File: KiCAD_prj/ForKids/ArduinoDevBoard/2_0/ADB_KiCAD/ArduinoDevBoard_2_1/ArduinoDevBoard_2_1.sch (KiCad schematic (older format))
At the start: 45 parts, among them J1 Conn_01x04_Female, J10 Conn_01x04_Female, J11 Conn_01x04_Female, J12 Conn_01x02_Female, J13 Conn_01x15_Female, J14 Conn_01x15_Female, J15 Conn_01x03_Female, J16 Conn_01x02_Female, J17 Conn_01x02_Female, J18 Conn_01x02_Female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

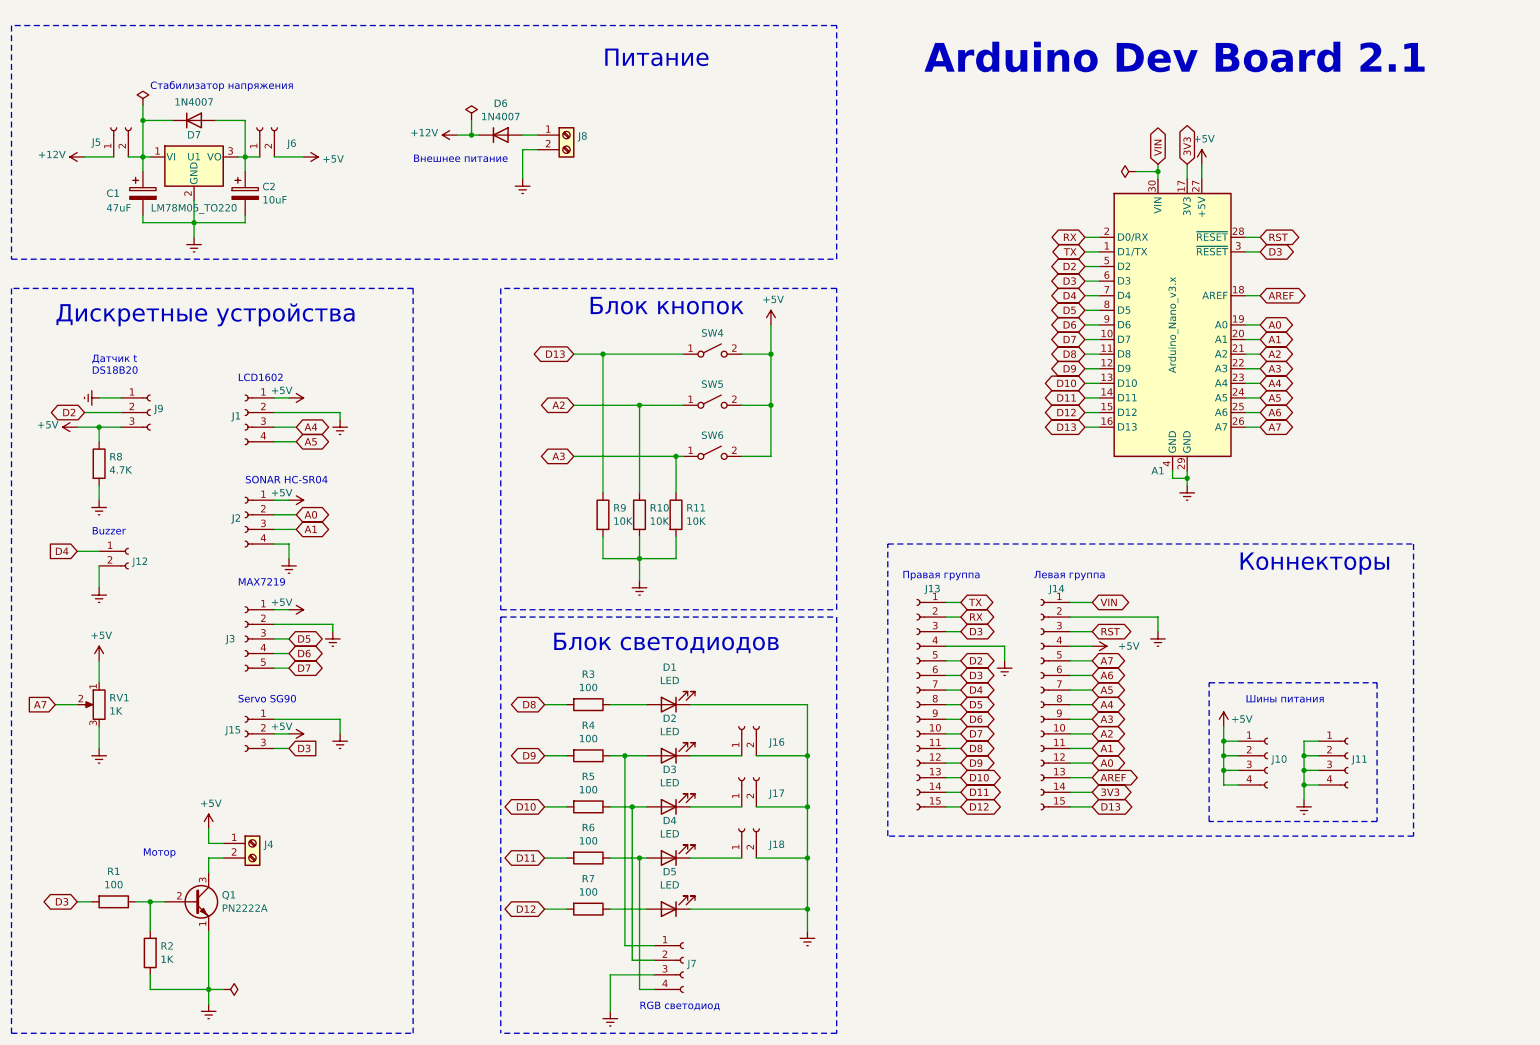
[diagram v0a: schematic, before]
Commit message: Update Arduino Dev Board 2.1
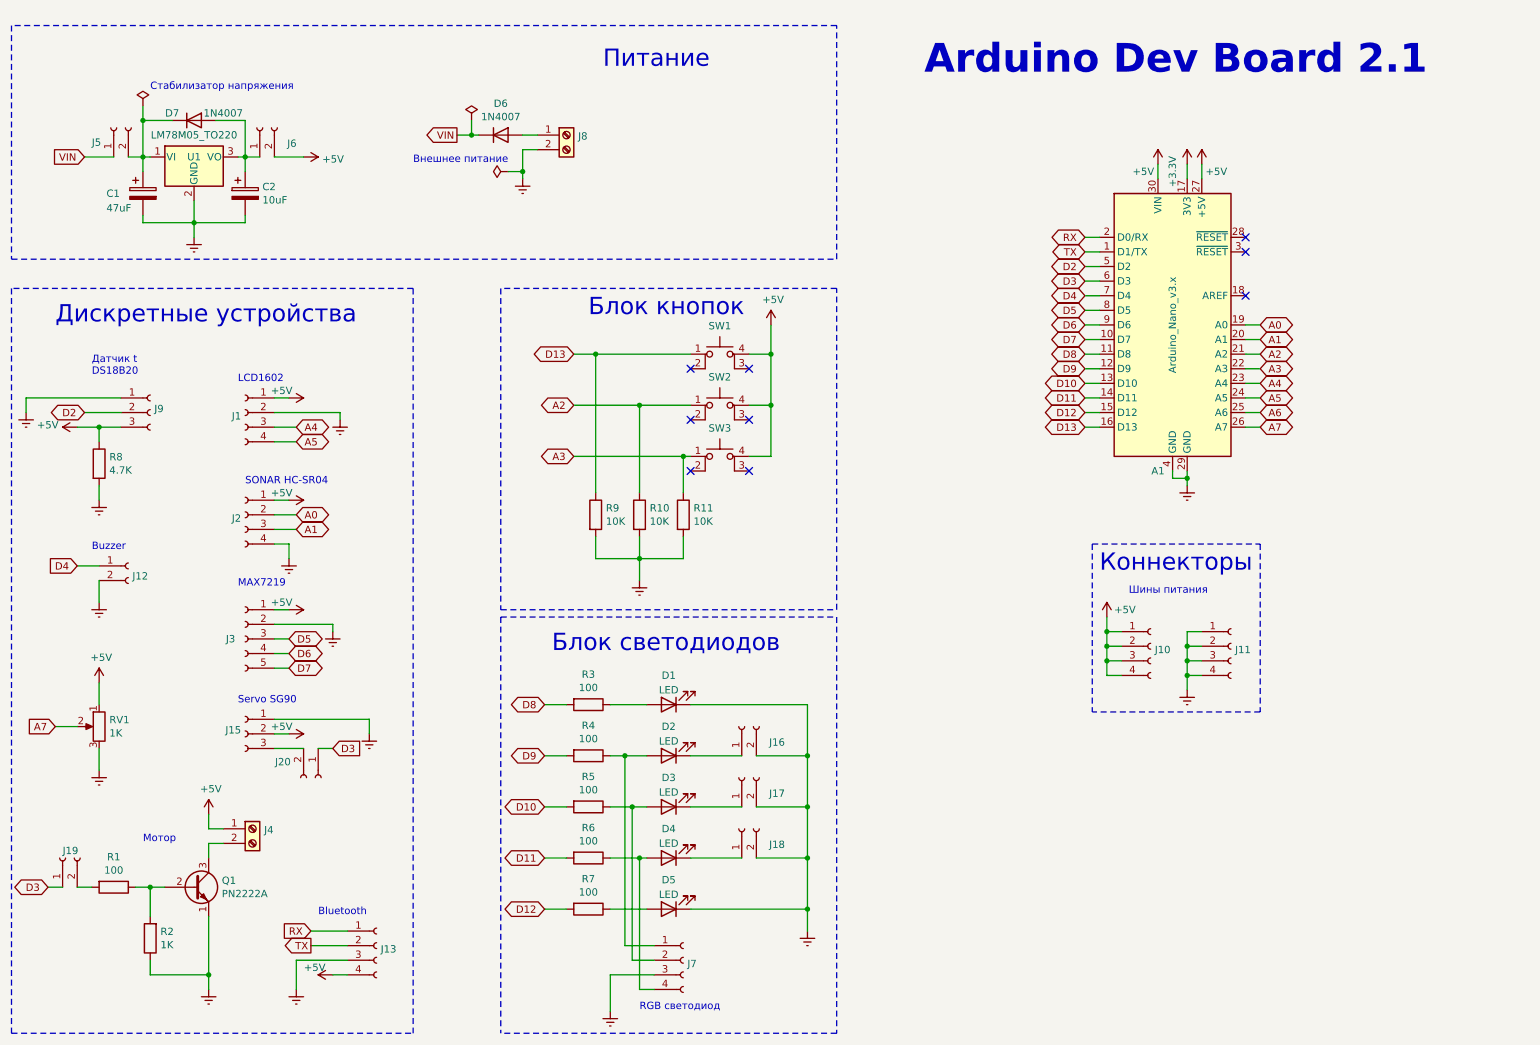
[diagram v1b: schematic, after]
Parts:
- removed J13, J14: Conn_01x15_Female, Connector_PinSocket_2.54mm:PinSocket_1x15_P2.54mm_Vertical, symbol Connector:Conn_01x15_Female
- removed SW4, SW5, SW6: SW_SPST, Button_Switch_THT:SW_PUSH_6mm_H5mm, symbol Switch:SW_SPST
- added J13: Conn_01x04_Female, Connector_PinHeader_2.54mm:PinHeader_1x04_P2.54mm_Vertical, symbol Connector:Conn_01x04_Female
- added J19, J20: Conn_01x02_Female, Connector_PinHeader_2.54mm:PinHeader_1x02_P2.54mm_Vertical, symbol Connector:Conn_01x02_Female
- added SW1, SW2, SW3: Button_Switch_THT:SW_PUSH_6mm_H5mm, Button_Switch_THT:SW_PUSH_6mm, symbol Switch:SW_MEC_5E
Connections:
- net +12V is gone; now on net VIN: D6.1 (K), J5.1 (Pin_1)
- net +5V: now also A1.30 (VIN), J13.4 (Pin_4), SW1.4 (A), SW2.4 (A), SW3.4 (A)
- net A2: now also SW2.1
- net A3: now also SW3.1
- net D13: now also SW1.1
- net D3: now also J19.1 (Pin_1), J20.1 (Pin_1); no longer A1.3 (~RESET), J15.3 (Pin_3), R1.2
- net Earth: now also J13.3 (Pin_3)
- net RX: now also J13.1 (Pin_1)
- net TX: now also J13.2 (Pin_2)
- net VIN: no longer A1.30 (VIN)
- net 3V3 renamed +3V3
- net AREF: no longer names the net of A1.18 (AREF)
- net RST: no longer names the net of A1.28 (~RESET)
- new net: J19.2 (Pin_2), R1.2
- new net: J15.3 (Pin_3), J20.2 (Pin_2)
- no-connect marks 0 -> 9
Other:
- note added: "Bluetooth"
- note removed: "Левая группа"
- note removed: "Правая группа"
- moved on the sheet: J10, J11, J12, J4, Q1, R1, R11, R2, R9, RV1

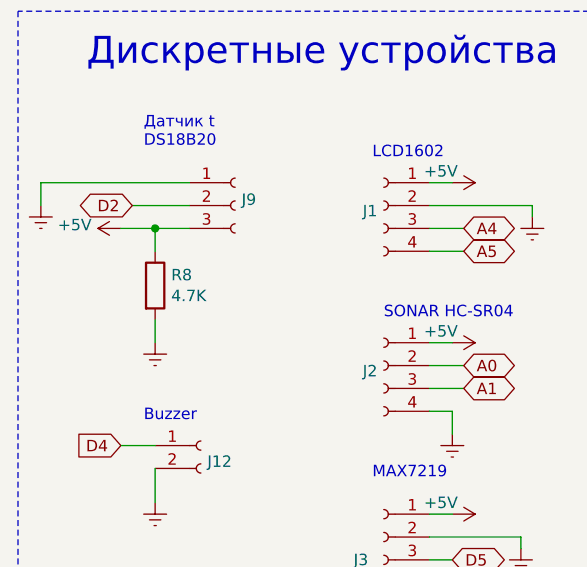
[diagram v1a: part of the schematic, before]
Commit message: Update Arduino Dev Board 2.1 fix resistor 4.7K
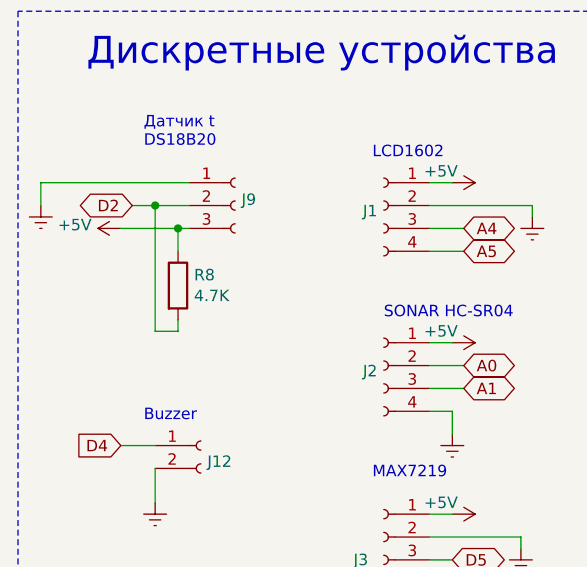
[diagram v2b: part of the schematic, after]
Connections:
- net D2: now also R8.2
- net Earth: no longer R8.2
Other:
- moved on the sheet: R8
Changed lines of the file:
@@
 L Device:R R8
 U 1 1 5DFDE4CA
-P 1600 3700
-F 0 "R8" H 1670 3746 50  0000 L CNN
-F 1 "4.7K" H 1670 3655 50  0000 L CNN
-F 2 "Resistor_THT:R_Axial_DIN0411_L9.9mm_D3.6mm_P12.70mm_Horizontal" V 1530 3700 50  0001 C CNN
-F 3 "~" H 1600 3700 50  0001 C CNN
-	1    1600 3700
-	1    0    0    -1
-$EndComp
-Wire Wire Line
-	1750 3450 1600 3450
-Wire Wire Line
-	1600 3450 1600 3550
+P 1700 3700
+F 0 "R8" H 1770 3746 50  0000 L CNN
+F 1 "4.7K" H 1770 3655 50  0000 L CNN
+F 2 "Resistor_THT:R_Axial_DIN0411_L9.9mm_D3.6mm_P12.70mm_Horizontal" V 1630 3700 50  0001 C CNN
+F 3 "~" H 1700 3700 50  0001 C CNN
+	1    1700 3700
+	1    0    0    -1
+$EndComp
 $Comp
 L power:+5V #PWR019
@@
 	0    -1   -1   0
 $EndComp
-Wire Wire Line
-	1450 3450 1600 3450
-Connection ~ 1600 3450
 Text GLabel 1500 3350 0    50   BiDi ~ 0
 D2
 Wire Wire Line
-	1750 3350 1500 3350
+	1750 3350 1600 3350
 $Comp
 L power:Earth #PWR020
@@
 	9550 2950 9450 2950
 $Comp
-L power:Earth #PWR021
-U 1 1 5E01E177
-P 1600 3950
-F 0 "#PWR021" H 1600 3700 50  0001 C CNN
-F 1 "Earth" H 1600 3800 50  0001 C CNN
-F 2 "" H 1600 3950 50  0001 C CNN
-F 3 "~" H 1600 3950 50  0001 C CNN
-	1    1600 3950
-	1    0    0    -1
-$EndComp
-Wire Wire Line
-	1600 3950 1600 3850
-$Comp
 L Device:LED D1
 U 1 1 5E023966
@@
 	1    0    0    -1
 $EndComp
+Wire Wire Line
+	1450 3450 1700 3450
+Wire Wire Line
+	1700 3550 1700 3450
+Connection ~ 1700 3450
+Wire Wire Line
+	1700 3450 1750 3450
+Wire Wire Line
+	1700 3850 1700 3900
+Wire Wire Line
+	1700 3900 1600 3900
+Wire Wire Line
+	1600 3900 1600 3350
+Connection ~ 1600 3350
+Wire Wire Line
+	1600 3350 1500 3350
 $EndSCHEMATC

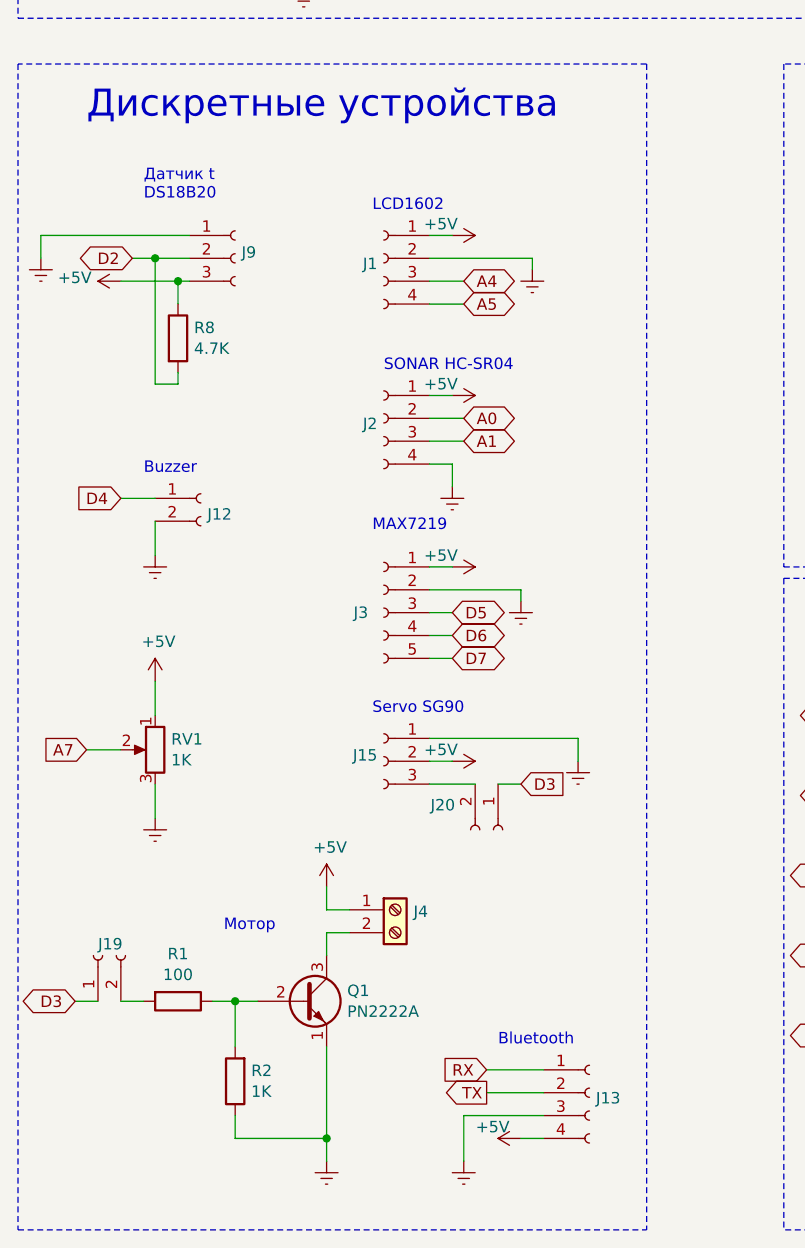
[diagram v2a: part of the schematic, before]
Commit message: Update Arduino Dev Board 2.0 KiCAD project: A6 -> sens t. D2 - free
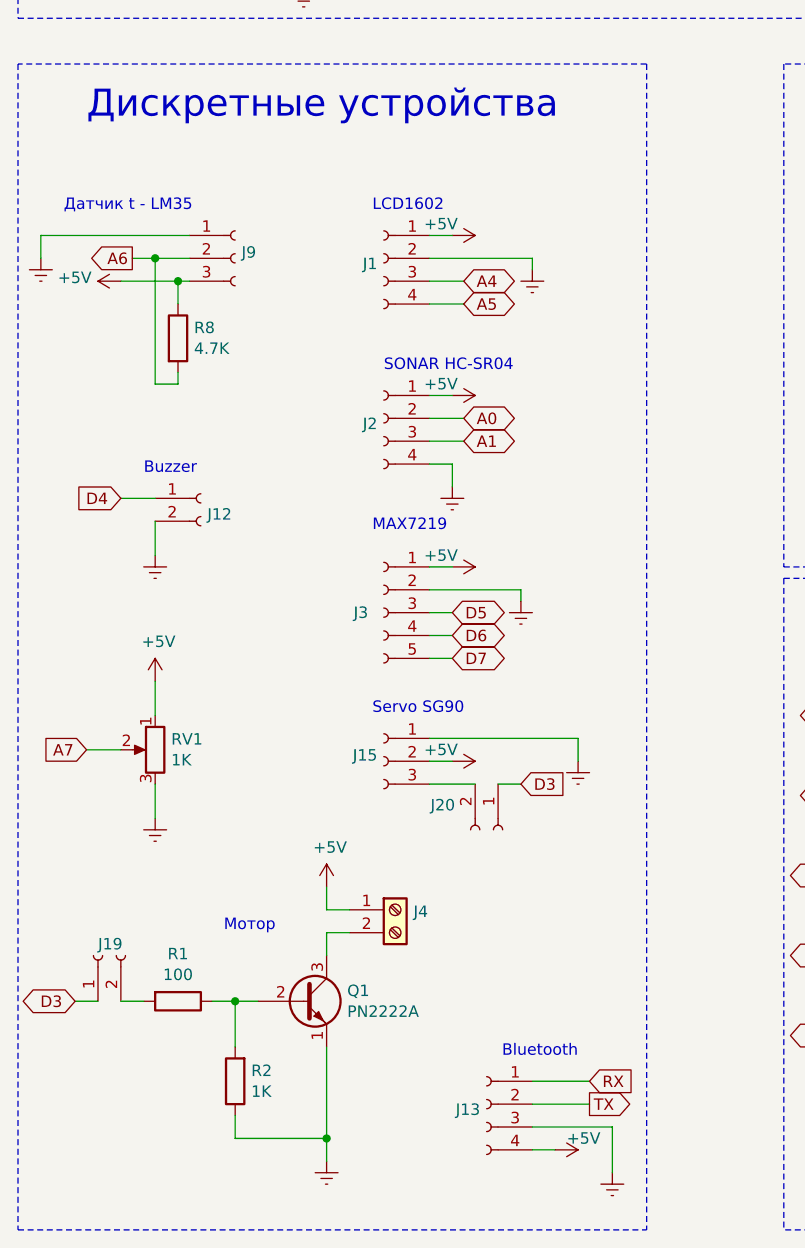
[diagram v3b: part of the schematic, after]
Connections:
- net A6: now also J9.2 (Pin_2), R8.2
- net D2: no longer J9.2 (Pin_2), R8.2
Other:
- note added: "Датчик t - LM35"
- note removed: "Датчик t\nDS18B20"
- moved on the sheet: J13
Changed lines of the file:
@@
 	0    -1   -1   0
 $EndComp
-Text GLabel 1500 3350 0    50   BiDi ~ 0
-D2
 Wire Wire Line
 	1750 3350 1600 3350
@@
 Text Notes 1950 1150 0    50   ~ 0
 Стабилизатор напряжения
-Text Notes 1550 3100 0    50   ~ 0
-Датчик t\nDS18B20
+Text Notes 1200 3150 0    50   ~ 0
+Датчик t - LM35
 $Comp
 L Connector:Screw_Terminal_01x02 J8
@@
 L Connector:Conn_01x04_Female J13
 U 1 1 60046ECC
-P 3500 7000
-F 0 "J13" H 3528 6976 50  0000 L CNN
-F 1 "Conn_01x04_Female" H 3528 6885 50  0001 L CNN
-F 2 "Connector_PinHeader_2.54mm:PinHeader_1x04_P2.54mm_Vertical" H 3500 7000 50  0001 C CNN
-F 3 "~" H 3500 7000 50  0001 C CNN
-	1    3500 7000
-	1    0    0    -1
+P 3050 7050
+F 0 "J13" H 3078 7026 50  0000 L CNN
+F 1 "Conn_01x04_Female" H 3078 6935 50  0001 L CNN
+F 2 "Connector_PinHeader_2.54mm:PinHeader_1x04_P2.54mm_Vertical" H 3050 7050 50  0001 C CNN
+F 3 "~" H 3050 7050 50  0001 C CNN
+	1    3050 7050
+	-1   0    0    -1
 $EndComp
 $Comp
 L power:Earth #PWR0101
 U 1 1 60048ECB
-P 2950 7300
-F 0 "#PWR0101" H 2950 7050 50  0001 C CNN
-F 1 "Earth" H 2950 7150 50  0001 C CNN
-F 2 "" H 2950 7300 50  0001 C CNN
-F 3 "~" H 2950 7300 50  0001 C CNN
-	1    2950 7300
-	1    0    0    -1
+P 3600 7350
+F 0 "#PWR0101" H 3600 7100 50  0001 C CNN
+F 1 "Earth" H 3600 7200 50  0001 C CNN
+F 2 "" H 3600 7350 50  0001 C CNN
+F 3 "~" H 3600 7350 50  0001 C CNN
+	1    3600 7350
+	-1   0    0    -1
 $EndComp
 $Comp
 L power:+5V #PWR0102
 U 1 1 60049990
-P 3200 7200
-F 0 "#PWR0102" H 3200 7050 50  0001 C CNN
-F 1 "+5V" V 3250 7250 50  0000 L CNN
-F 2 "" H 3200 7200 50  0001 C CNN
-F 3 "" H 3200 7200 50  0001 C CNN
-	1    3200 7200
-	0    -1   -1   0
-$EndComp
-Wire Wire Line
-	3200 7200 3300 7200
-Wire Wire Line
-	3300 7100 2950 7100
-Wire Wire Line
-	2950 7100 2950 7300
-Text GLabel 3050 6900 0    50   Input ~ 0
+P 3350 7250
+F 0 "#PWR0102" H 3350 7100 50  0001 C CNN
+F 1 "+5V" V 3400 7300 50  0000 L CNN
+F 2 "" H 3350 7250 50  0001 C CNN
+F 3 "" H 3350 7250 50  0001 C CNN
+	1    3350 7250
+	0    1    -1   0
+$EndComp
+Wire Wire Line
+	3350 7250 3250 7250
+Wire Wire Line
+	3250 7150 3600 7150
+Wire Wire Line
+	3600 7150 3600 7350
+Text GLabel 3500 6950 2    50   Input ~ 0
 RX
 Wire Wire Line
-	3050 6900 3300 6900
-Text GLabel 3050 7000 0    50   Output ~ 0
+	3500 6950 3250 6950
+Text GLabel 3500 7050 2    50   Output ~ 0
 TX
 Wire Wire Line
-	3050 7000 3300 7000
-Text Notes 3100 6800 0    50   ~ 0
+	3500 7050 3250 7050
+Text Notes 3450 6850 2    50   ~ 0
 Bluetooth
 Wire Notes Line
@@
 Wire Wire Line
 	1600 3350 1500 3350
+Text GLabel 1500 3350 0    50   Output ~ 0
+A6
 $EndSCHEMATC

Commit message: Update ArduinoDevBoard 2.1 project
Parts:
- removed J19: Conn_01x02_Female, Connector_PinHeader_2.54mm:PinHeader_1x02_P2.54mm_Vertical, symbol Connector:Conn_01x02_Female
- removed Q1: PN2222A, Package_TO_SOT_THT:TO-92_Inline_Wide, symbol Transistor_BJT:PN2222A
- removed R1: 100, Resistor_THT:R_Axial_DIN0411_L9.9mm_D3.6mm_P12.70mm_Horizontal, symbol Device:R
- removed R2: 1K, Resistor_THT:R_Axial_DIN0411_L9.9mm_D3.6mm_P12.70mm_Horizontal, symbol Device:R
- removed SW1, SW2, SW3: Button_Switch_THT:SW_PUSH_6mm_H5mm, Button_Switch_THT:SW_PUSH_6mm, symbol Switch:SW_MEC_5E
- added J14: M-PWM, Connector_PinHeader_2.54mm:PinHeader_1x02_P2.54mm_Vertical, symbol Connector:Conn_01x02_Female
- added SW1, SW2, SW3: SW_Push_Dual, Button_Switch_THT:SW_PUSH_6mm, symbol Switch:SW_Push_Dual
- J1: value Conn_01x04_Female -> LCD1602
- J10: value Conn_01x04_Female -> +5V
- J11: value Conn_01x04_Female -> GND
- J12: value Conn_01x02_Female -> Buzzer
- J13: value Conn_01x04_Female -> Bluetooth
- J15: value Conn_01x03_Female -> Servo SG90
- J2: value Conn_01x04_Female -> HC-SR04
- J20: value Conn_01x02_Female -> M
- J3: value Conn_01x05_Female -> MAX7219
- J4: value Screw_Terminal_01x02 -> MOTOR; footprint Connector_Phoenix_MC:PhoenixContact_MCV_1,5_2-G-3.5_1x02_P3.50mm_Vertical -> Connector_PinHeader_2.54mm:PinHeader_1x02_P2.54mm_Vertical
- J8: value Screw_Terminal_01x02 -> OUT POWER
- J9: value Conn_01x03_Female -> LM35
- R8: value 4.7K -> 10K
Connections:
- net +5V: now also J9.1 (Pin_1), SW1.2, SW2.2, SW3.2; no longer J4.1 (Pin_1), J9.3 (Pin_3), R8.1
- net A2: now also SW2.1
- net A3: now also SW3.1
- net A6: now also R8.1; no longer R8.2
- net D13: now also SW1.1
- net D2: now also J4.2 (Pin_2)
- net D3: now also J14.1 (Pin_1)
- net Earth: now also J9.3 (Pin_3), R8.2; no longer J9.1 (Pin_1)
- net +3V3: no longer names the net of A1.17 (3V3)
- new net: J14.2 (Pin_2), J4.1 (Pin_1)
- no-connect marks 9 -> 10
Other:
- moved on the sheet: J4, R10, R11, R8, R9

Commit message: Update ArduinoDevBoard 2.1. Upgrade pcb
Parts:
- J8: value OUT POWER -> VIN <= 12V
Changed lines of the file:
@@
 	-1   0    0    -1
 $EndComp
-Text GLabel 1550 6750 0    50   BiDi ~ 0
+Text GLabel 1550 6750 0    50   Output ~ 0
 D3
 $Comp
@@
 P 4800 1450
 F 0 "J8" H 4880 1442 50  0000 L CNN
-F 1 "OUT POWER" H 4880 1351 50  0000 L CNN
+F 1 "VIN <= 12V" H 4880 1351 50  0000 L CNN
 F 2 "Connector_Phoenix_MC:PhoenixContact_MCV_1,5_2-G-3.5_1x02_P3.50mm_Vertical" H 4800 1450 50  0001 C CNN
 F 3 "~" H 4800 1450 50  0001 C CNN
